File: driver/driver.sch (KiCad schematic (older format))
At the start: 105 parts, among them J1 OUT_A, J10 FAN, J2 OUT_B, J3 UART_DEBUG, J4 USB_B_Micro, J5 CH340E module, J6 1602 I2C LCD, J7 IN_VCC, J8 IN_GND, J9 SWD, Q1 TPHR6503PL, Q2 TPHR6503PL, Q3 TPHR6503PL, Q4 TPHR6503PL, SW1 SW_Push, SW2 SW_Push, U1 MT3608, U10 PC817, U2 AMS1117-5.0, U3 AMS1117-3.3, U4 TC4427, U5 TC4427, U6 STM32F103C8Tx, U7 INA226, U8 MCP9804_MSOP, U9 PC817, Y1 8MHz

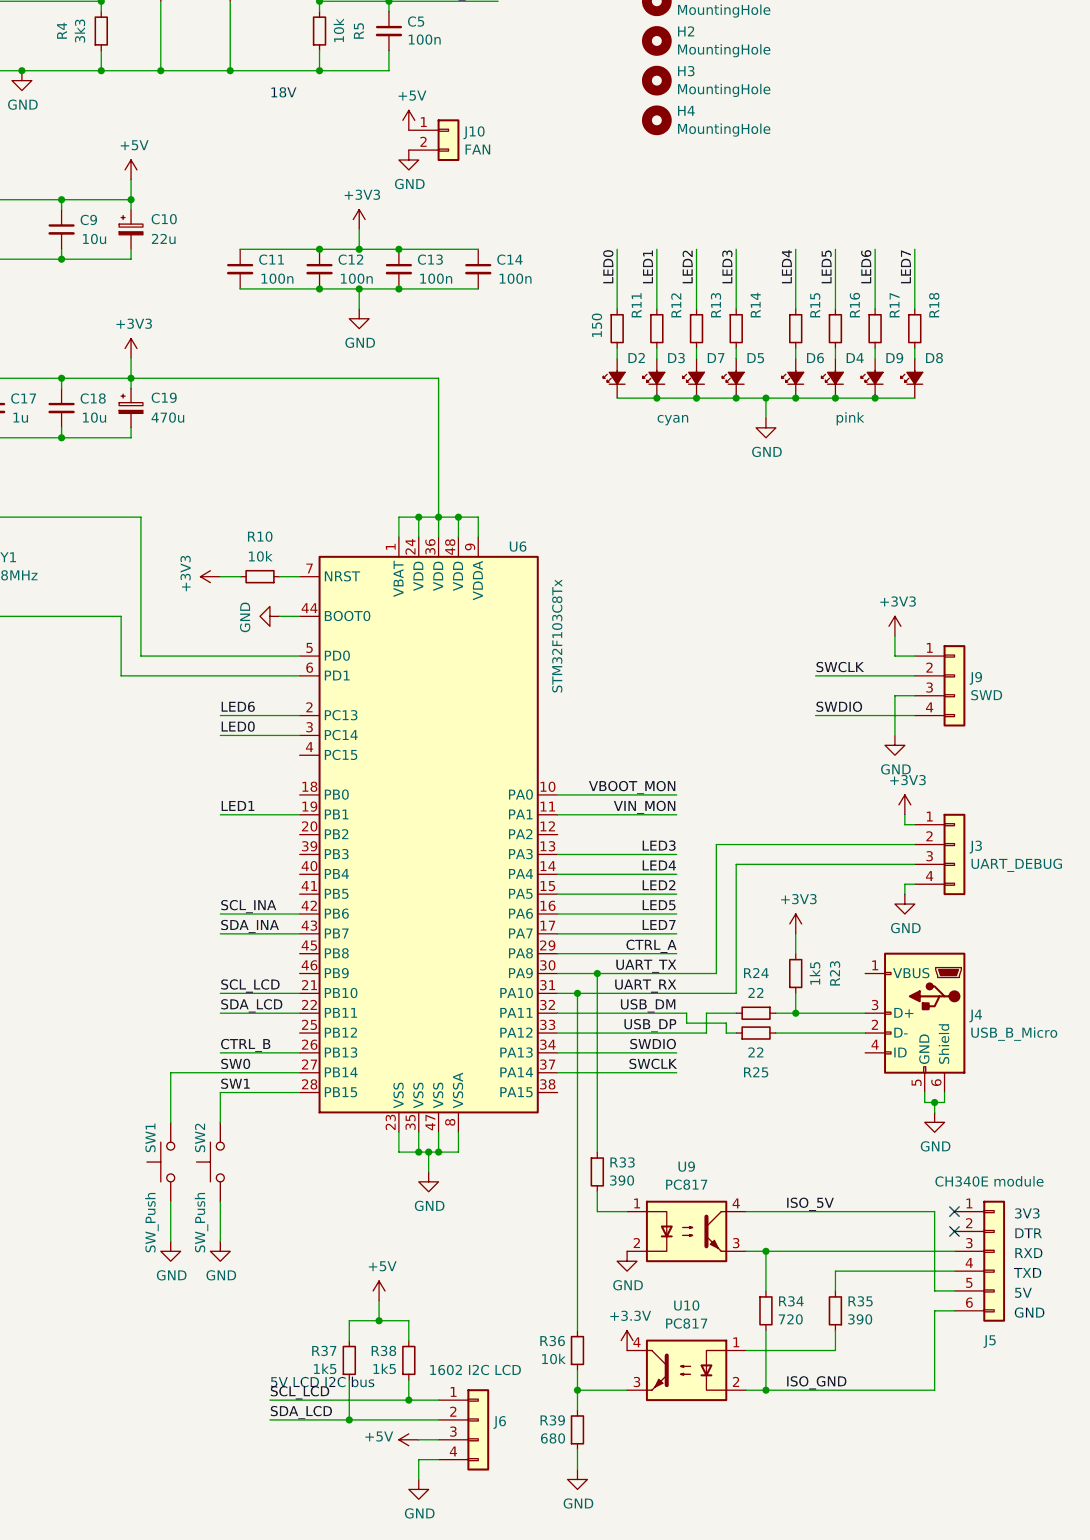
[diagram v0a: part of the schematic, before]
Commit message: driver: Add mounting holes for RS485 adapter
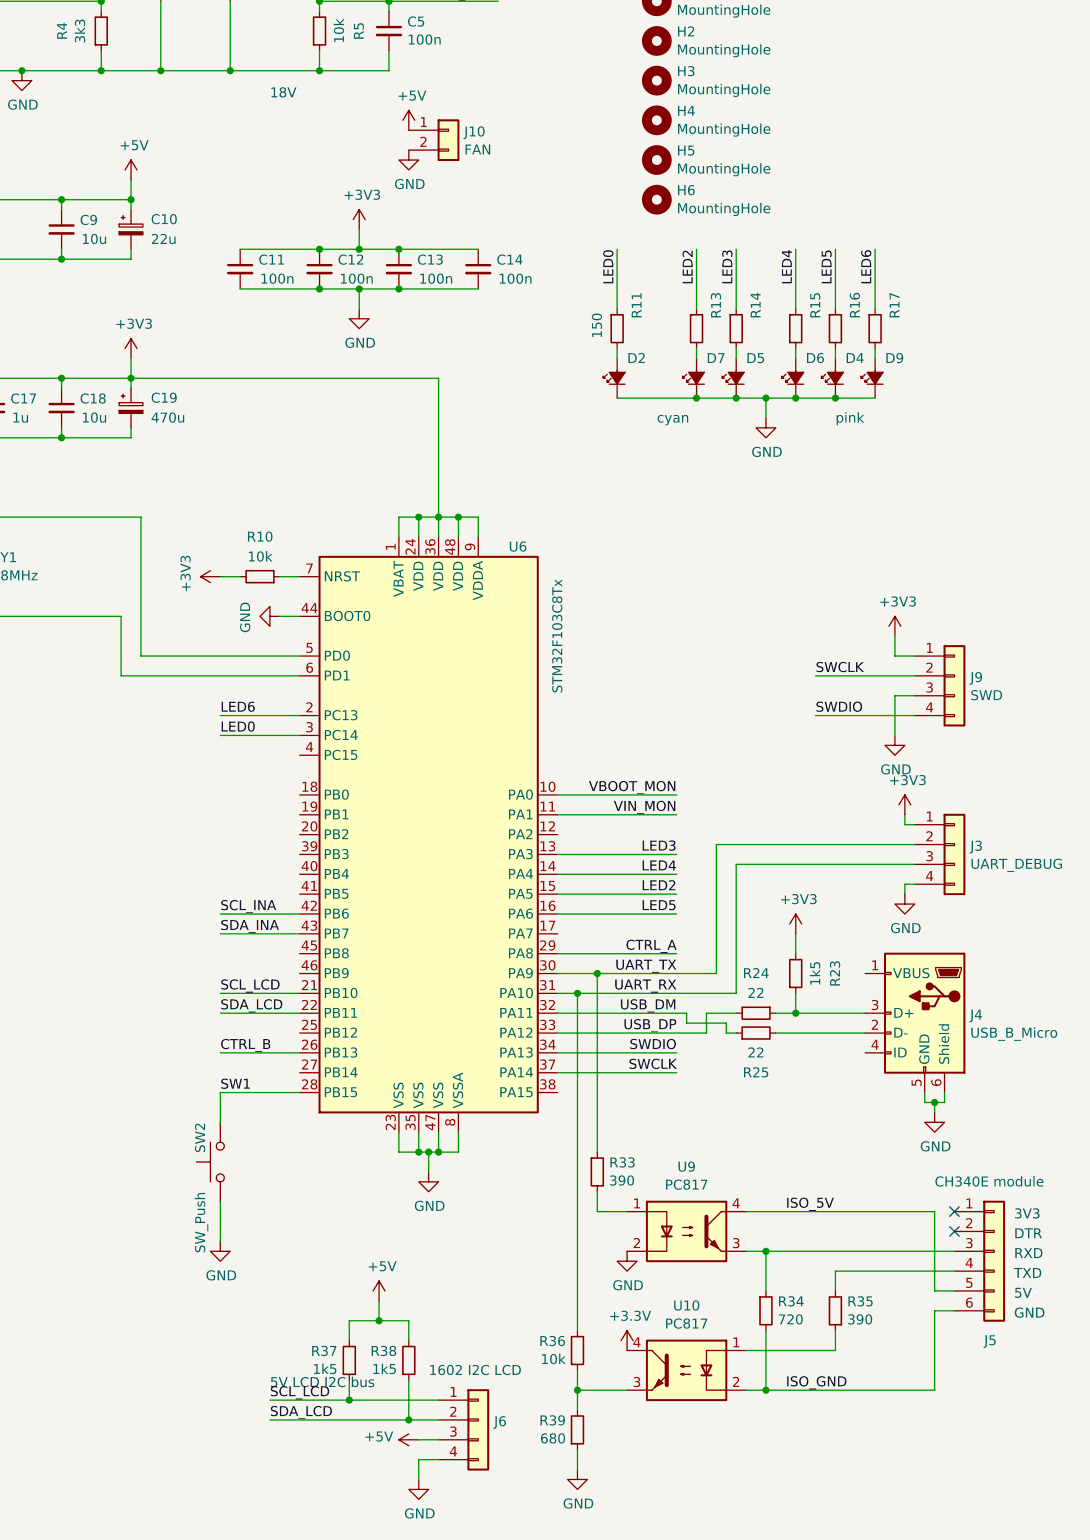
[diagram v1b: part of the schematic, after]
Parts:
- removed D3: cyan, LED_SMD:LED_PLCC_2835_Handsoldering, symbol Device:LED_Small_ALT
- removed D8: pink, LED_SMD:LED_PLCC_2835_Handsoldering, symbol Device:LED_Small_ALT
- removed R12, R18: 150, Resistor_SMD:R_0603_1608Metric_Pad1.05x0.95mm_HandSolder, symbol Device:R_Small
- removed SW1: SW_Push, Button_Switch_THT:SW_PUSH_6mm, symbol Switch:SW_Push
- added H5, H6: MountingHole, MountingHole:MountingHole_3.2mm_M3, symbol Mechanical:MountingHole
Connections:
- net SCL_LCD: now also R37.1; no longer R38.1
- net SDA_LCD: now also R38.1; no longer R37.1
- net LED1: no longer names the net of U6.19 (PB1)
- net LED7: no longer names the net of U6.17 (PA7)
- net SW0: no longer names the net of U6.27 (PB14)
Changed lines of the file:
@@
 Wire Wire Line
 	16550 9550 16650 9550
-Wire Wire Line
-	16500 9250 16650 9250
 $Comp
 L Device:R_Small R26
@@
 	1    0    0    1
 $EndComp
-Wire Wire Line
-	16200 9350 16650 9350
-Wire Wire Line
-	16200 9150 16200 9350
-Wire Wire Line
-	16500 9150 16500 9250
 $Comp
 L power:+5V #PWR0136
@@
 Wire Wire Line
 	16550 9450 16650 9450
-Connection ~ 16500 9250
-Connection ~ 16200 9350
 Text Label 15800 9350 0    50   ~ 0
 SDA_LCD
 Text Label 15800 9250 0    50   ~ 0
 SCL_LCD
-Wire Wire Line
-	15800 9250 16500 9250
-Wire Wire Line
-	15800 9350 16200 9350
 Text Notes 15800 9200 0    50   ~ 0
 5V LCD I2C bus
@@
 $EndComp
 $Comp
-L Device:LED_Small_ALT D3
-U 1 1 5D1201FD
-P 17750 4100
-F 0 "D3" V 17850 4050 50  0000 R CNN
-F 1 "cyan" V 17705 4032 50  0001 R CNN
-F 2 "LED_SMD:LED_PLCC_2835_Handsoldering" V 17750 4100 50  0001 C CNN
-F 3 "~" V 17750 4100 50  0001 C CNN
-	1    17750 4100
-	0    -1   -1   0
-$EndComp
-$Comp
 L Device:LED_Small_ALT D4
 U 1 1 5D120495
@@
 $EndComp
 $Comp
-L Device:LED_Small_ALT D8
-U 1 1 5D1365C9
-P 19050 4100
-F 0 "D8" V 19150 4050 50  0000 R CNN
-F 1 "pink" V 19005 4032 50  0001 R CNN
-F 2 "LED_SMD:LED_PLCC_2835_Handsoldering" V 19050 4100 50  0001 C CNN
-F 3 "~" V 19050 4100 50  0001 C CNN
-	1    19050 4100
-	0    -1   -1   0
-$EndComp
-$Comp
 L Device:LED_Small_ALT D9
 U 1 1 5D138D62
@@
 $EndComp
 $Comp
-L Device:R_Small R12
-U 1 1 5D18C65D
-P 17750 3850
-F 0 "R12" V 17850 3900 50  0000 L CNN
-F 1 "150" V 17650 3800 50  0001 L CNN
-F 2 "Resistor_SMD:R_0603_1608Metric_Pad1.05x0.95mm_HandSolder" H 17750 3850 50  0001 C CNN
-F 3 "~" H 17750 3850 50  0001 C CNN
-	1    17750 3850
-	1    0    0    -1
-$EndComp
-$Comp
 L Device:R_Small R13
 U 1 1 5D18F534
@@
 	1    0    0    -1
 $EndComp
-$Comp
-L Device:R_Small R18
-U 1 1 5D191497
-P 19050 3850
-F 0 "R18" V 19150 3900 50  0000 L CNN
-F 1 "150" V 18950 3800 50  0001 L CNN
-F 2 "Resistor_SMD:R_0603_1608Metric_Pad1.05x0.95mm_HandSolder" H 19050 3850 50  0001 C CNN
-F 3 "~" H 19050 3850 50  0001 C CNN
-	1    19050 3850
-	1    0    0    -1
-$EndComp
-Wire Wire Line
-	19050 3950 19050 4000
 Wire Wire Line
 	18850 3950 18850 4000
@@
 	17950 3950 17950 4000
 Wire Wire Line
-	17750 4000 17750 3950
-Wire Wire Line
 	17550 3950 17550 4000
-Wire Wire Line
-	17550 4200 17750 4200
-Connection ~ 17750 4200
-Wire Wire Line
-	17750 4200 17950 4200
 Connection ~ 17950 4200
 Wire Wire Line
@@
 Wire Wire Line
 	18650 4200 18850 4200
-Connection ~ 18850 4200
-Wire Wire Line
-	18850 4200 19050 4200
 $Comp
 L power:GND #PWR0141
@@
 Wire Wire Line
 	18300 4200 18450 4200
-Text Label 17750 3450 3    50   ~ 0
-LED1
 Text Label 17550 3450 3    50   ~ 0
 LED0
@@
 Text Label 18850 3450 3    50   ~ 0
 LED6
-Text Label 19050 3450 3    50   ~ 0
-LED7
-Wire Wire Line
-	19050 3450 19050 3750
 Wire Wire Line
 	18850 3750 18850 3450
@@
 Wire Wire Line
 	17950 3450 17950 3750
-Wire Wire Line
-	17750 3750 17750 3450
 Wire Wire Line
 	17550 3450 17550 3750
 Text Label 15550 5900 0    50   ~ 0
 LED0
-Text Label 15550 6300 0    50   ~ 0
-LED1
 Text Label 17850 6700 2    50   ~ 0
 LED2
@@
 Text Label 15550 5800 0    50   ~ 0
 LED6
-Text Label 17850 6900 2    50   ~ 0
-LED7
-Wire Wire Line
-	17850 6900 17250 6900
 Wire Wire Line
 	17250 6800 17850 6800
@@
 Wire Wire Line
 	17250 6600 17850 6600
-Wire Wire Line
-	15950 6300 15550 6300
-$Comp
-L Switch:SW_Push SW1
-U 1 1 5D5D8224
-P 15300 8050
-F 0 "SW1" H 15500 8150 50  0000 R CNN
-F 1 "SW_Push" H 15150 8150 50  0000 R CNN
-F 2 "Button_Switch_THT:SW_PUSH_6mm" H 15300 8250 50  0001 C CNN
-F 3 "" H 15300 8250 50  0001 C CNN
-	1    15300 8050
-	0    -1   -1   0
-$EndComp
-$Comp
-L power:GND #PWR0142
-U 1 1 5D5DDBEA
-P 15300 8450
-F 0 "#PWR0142" H 15300 8200 50  0001 C CNN
-F 1 "GND" H 15305 8277 50  0000 C CNN
-F 2 "" H 15300 8450 50  0001 C CNN
-F 3 "" H 15300 8450 50  0001 C CNN
-	1    15300 8450
-	1    0    0    -1
-$EndComp
-Wire Wire Line
-	15300 8450 15300 8250
 $Comp
 L Switch:SW_Push SW2
@@
 Wire Wire Line
 	15550 7700 15550 7850
-Wire Wire Line
-	15950 7600 15300 7600
-Wire Wire Line
-	15300 7600 15300 7850
 Text Label 15550 7700 0    50   ~ 0
 SW1
-Text Label 15550 7600 0    50   ~ 0
-SW0
 $Comp
 L Sensor_Temperature:MCP9804_MSOP U8
@@
 	1    0    0    -1
 $EndComp
+$Comp
+L Mechanical:MountingHole H5
+U 1 1 5C529D2F
+P 17750 3000
+F 0 "H5" H 17850 3046 50  0000 L CNN
+F 1 "MountingHole" H 17850 2955 50  0000 L CNN
+F 2 "MountingHole:MountingHole_3.2mm_M3" H 17750 3000 50  0001 C CNN
+F 3 "~" H 17750 3000 50  0001 C CNN
+	1    17750 3000
+	1    0    0    -1
+$EndComp
+$Comp
+L Mechanical:MountingHole H6
+U 1 1 5C52B98B
+P 17750 3200
+F 0 "H6" H 17850 3246 50  0000 L CNN
+F 1 "MountingHole" H 17850 3155 50  0000 L CNN
+F 2 "MountingHole:MountingHole_3.2mm_M3" H 17750 3200 50  0001 C CNN
+F 3 "~" H 17750 3200 50  0001 C CNN
+	1    17750 3200
+	1    0    0    -1
+$EndComp
+Wire Wire Line
+	17550 4200 17950 4200
+Wire Wire Line
+	15800 9350 16500 9350
+Wire Wire Line
+	15800 9250 16200 9250
+Wire Wire Line
+	16500 9150 16500 9350
+Connection ~ 16500 9350
+Wire Wire Line
+	16500 9350 16650 9350
+Wire Wire Line
+	16200 9150 16200 9250
+Connection ~ 16200 9250
+Wire Wire Line
+	16200 9250 16650 9250
 $EndSCHEMATC
